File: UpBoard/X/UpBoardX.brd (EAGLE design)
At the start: 100 x 80 mm, 112 parts, among them CN1 100nF, CN2 100nF, CN3 100nF, CN4 100nF, IC1 SAM3X8E(ARDUINO), Q1 FDS5680, Q2 FDS5680, Q3 FDS5680, Q4 FDS5680

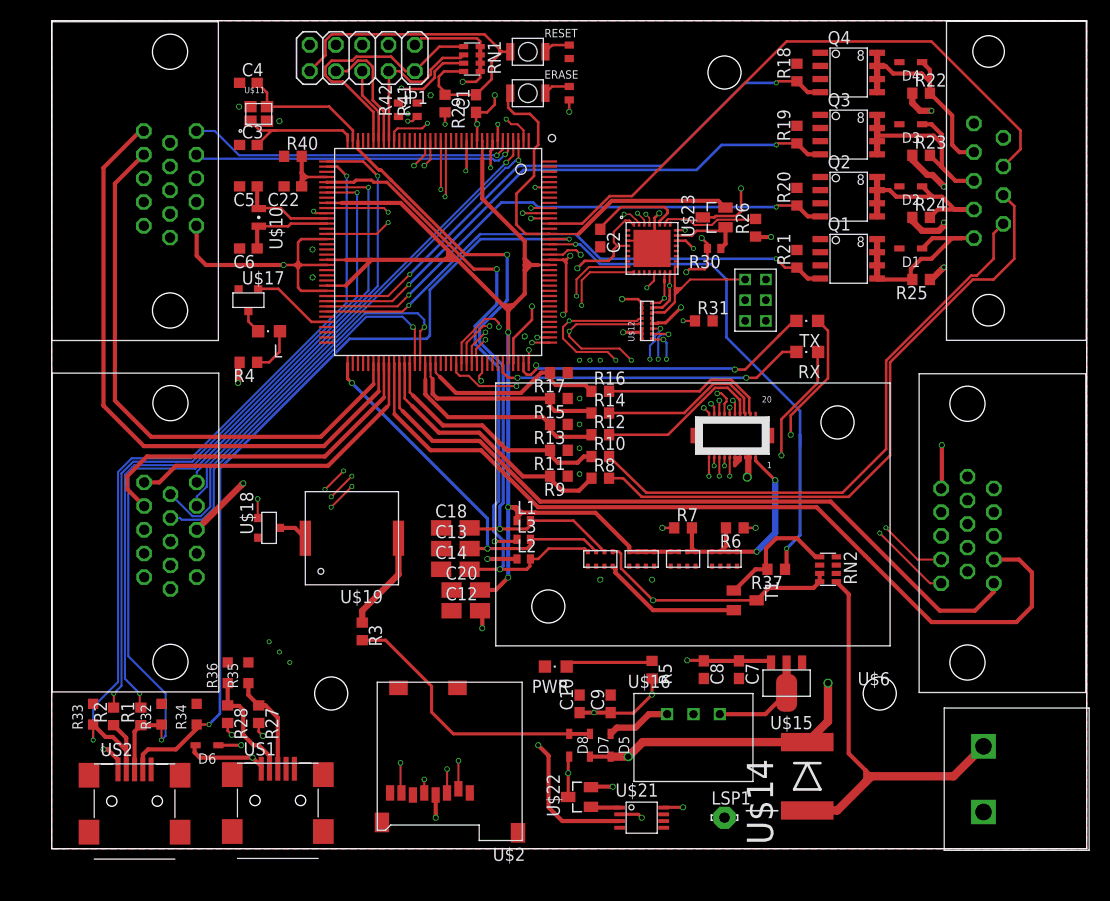
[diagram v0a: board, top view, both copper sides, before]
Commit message: Revised overly complicated power system
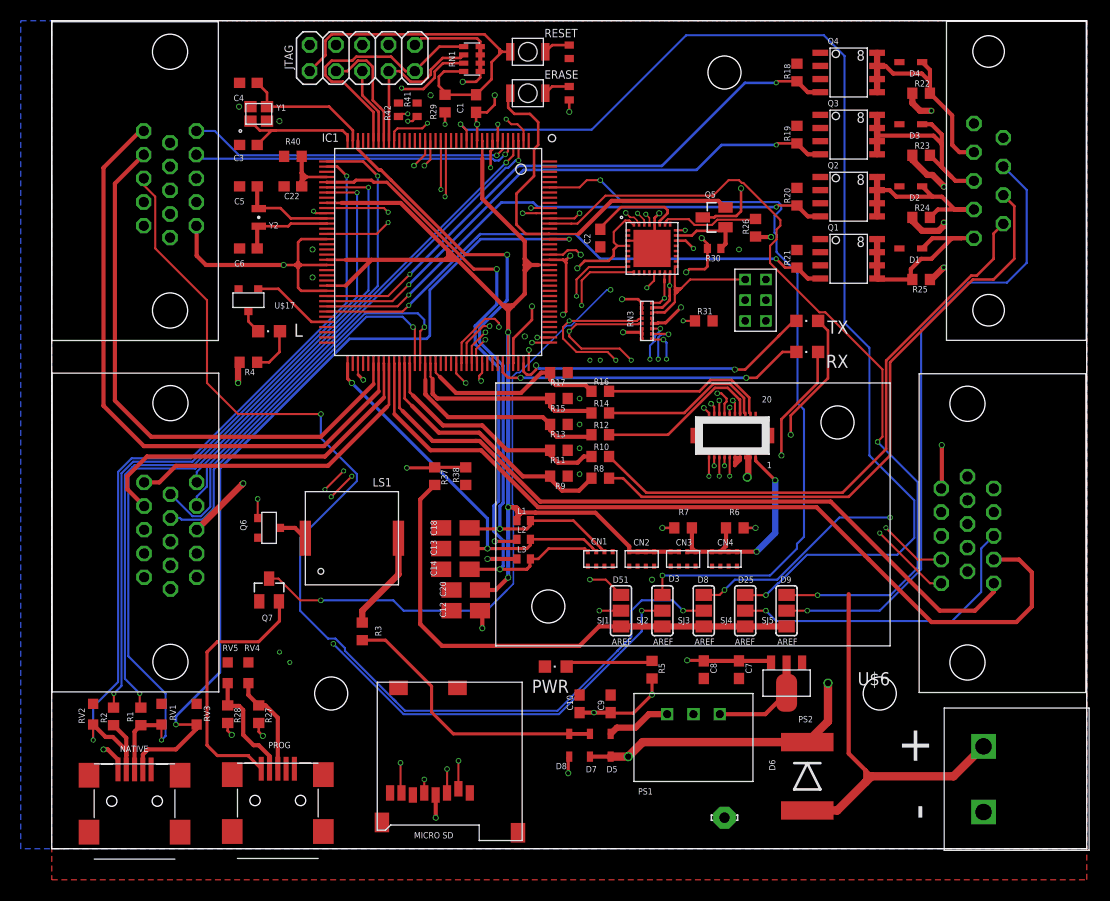
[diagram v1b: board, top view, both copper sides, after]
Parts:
- removed RN2: CTS742C083, resistor-net:CTS742C083
- removed T1: (no value), transistor:SOT23-BEC
- removed U$14: S10M-TP, UpBoard:DO-214AB
- removed U$21: OPAIC, linear:MICRO8
- removed U$22: SSMJ328R,LF, transistor-fet:SOT23
- added Q7: SSMJ328R,LF, transistor-fet:SOT23
- added R38: (no value), resistor:R0603
- added SJ1, SJ2, SJ3, SJ4, SJ5: (no value), jumper:SJ_2
- D6: value (none) -> S10M-TP; device zetex:SOD323 -> UpBoard:DO-214AB
- R37: value 1k -> (none)
- RN1: value CTS742C083 -> 10K
- RN3: value EXB-2HV102JV -> 1K
- moved D6 58.1 mm to (73.0, 7.00), turned to 90 degrees
- moved R37 34.2 mm to (37.0, 36.0), turned to 270 degrees
- moved CN4 12.0 mm to (65.0, 28.0), turned to 0 degrees
- moved CN1 4.00 mm to (53.0, 28.0), turned to 180 degrees
- moved CN2 4.00 mm to (57.0, 28.0)
- moved CN3 4.00 mm to (61.0, 28.0)
- moved L2 1.90 mm to (45.6, 29.9)
- moved L3 1.90 mm to (45.6, 28.0)
- renumbered R32 to RV1, R33 to RV2, R34 to RV3, R35 to RV4, R36 to RV5, U$10 to Y2, U$11 to Y1, U$12 to RN3, U$15 to PS2, U$16 to PS1, U$18 to Q6, U$19 to LS1, U$23 to Q5, US1 to PROG, US2 to NATIVE
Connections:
- removed net CMP: CN4.P$5, RN2.3, RN2.4, T1.C, U$21.3
- removed net CMP_GATE: R37.2, RN2.1, T1.B
- removed net N$25: U$21.1, U$22.1
- removed net N$31: CN4.P$1, T1.E
- new net AREF: R37.2, SJ1.3, SJ2.3, SJ3.3, SJ4.3, SJ5.3
- new net AREF0/D51: SJ1.2, U$6.P$16
- new net AREF1/D3: SJ2.2, U$3.13
- new net AREF2/D8: SJ3.2, U$4.13
- new net AREF3/D25: SJ4.2, U$8.13
- new net AREF4/D9: SJ5.2, U$5.7
- new net AVDREF: IC1.P$75, R37.1, R38.2
- new net N$5: Q7.3, U$1.P31
- net 1.8V: now also CN2.P$3, CN2.P$4, CN3.P$1, CN3.P$2; no longer CN1.P$1, CN1.P$2, CN1.P$3, CN1.P$4
- net 12V: now also D6.-; no longer U$14.-
- net 3.3V: now also CN4.P$1, CN4.P$2, CN4.P$3, CN4.P$4; no longer CN2.P$3, CN2.P$4, CN3.P$1, CN3.P$2, U$21.2
- net 5V: no longer D6.1, U$21.8, U$22.3
- net D25: now also SJ4.1; no longer U$8.13
- net D3: now also SJ2.1; no longer U$3.13
- net D51: now also SJ1.1; no longer U$6.P$16
- net D8: now also SJ3.1; no longer U$4.13
- net D9: now also SJ5.1; no longer U$5.7
- net GND: now also CN1.P$2, CN1.P$3, CN1.P$4, CN4.P$5, CN4.P$6, CN4.P$7, CN4.P$8, Q7.1, R38.1; no longer CN1.P$5, CN1.P$6, CN1.P$7, CN1.P$8, CN4.P$2, CN4.P$3, CN4.P$4, RN2.6, RN2.8, U$21.4
- net UOTGVBOF: no longer R37.1
- net VBUS: no longer U$22.2
- net VBUS_CFG: now also Q7.2; no longer D6.2, U$1.P31
- net VDDANA: now also CN1.P$7, L2.2; no longer CN4.P$7, L3.2
- net VDDPLL: now also CN1.P$6; no longer CN4.P$6
- net VDDUTMI: now also CN1.P$8, L3.2; no longer CN4.P$8, L2.2
- net VIN: now also D6.+; no longer RN2.5, U$14.+
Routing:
- net AREF2/D8: track 0.00 -> 107.1 mm, vias 0 -> 2
- net N$5: track 0.00 -> 68.9 mm, vias 0 -> 3
- net AREF1/D3: track 0.00 -> 63.3 mm, vias 0 -> 2
- net AREF4/D9: track 0.00 -> 60.9 mm, vias 0 -> 1
- net CMP: track 59.1 -> 0.00 mm, vias 2 -> 0
- net VBUS_CFG: track 83.6 -> 25.4 mm, vias 4 -> 0
- net UOTGVBOF: track 51.2 -> 0.00 mm, vias 2 -> 0
- net AREF: track 0.00 -> 51.1 mm
- net D25: track 71.6 -> 111.8 mm, vias 1 -> 2
- net D8: track 47.6 -> 85.3 mm, vias 1 -> 3
- net AREF0/D51: track 0.00 -> 30.8 mm, vias 0 -> 2
- net AREF3/D25: track 0.00 -> 30.3 mm, vias 0 -> 1
- net D9: track 60.5 -> 80.1 mm, vias 0 -> 2
- net AVDREF: track 0.00 -> 17.8 mm, vias 0 -> 2
- net D3: track 59.6 -> 74.6 mm, vias 3 -> 2
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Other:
- board text added: "+"
- board text added: "-"
- board text added: "AREF"
- board text added: "CN1"
- board text added: "CN2"
- board text added: "CN3"
- board text added: "CN4"
- board text added: "D25"
- board text added: "D3"
- board text added: "D51"
- board text added: "D8"
- board text added: "D9"
- board text added: "IC1"
- board text added: "JTAG"
- board text added: "LS1"
- board text added: "MICRO SD"

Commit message: Simplified power system
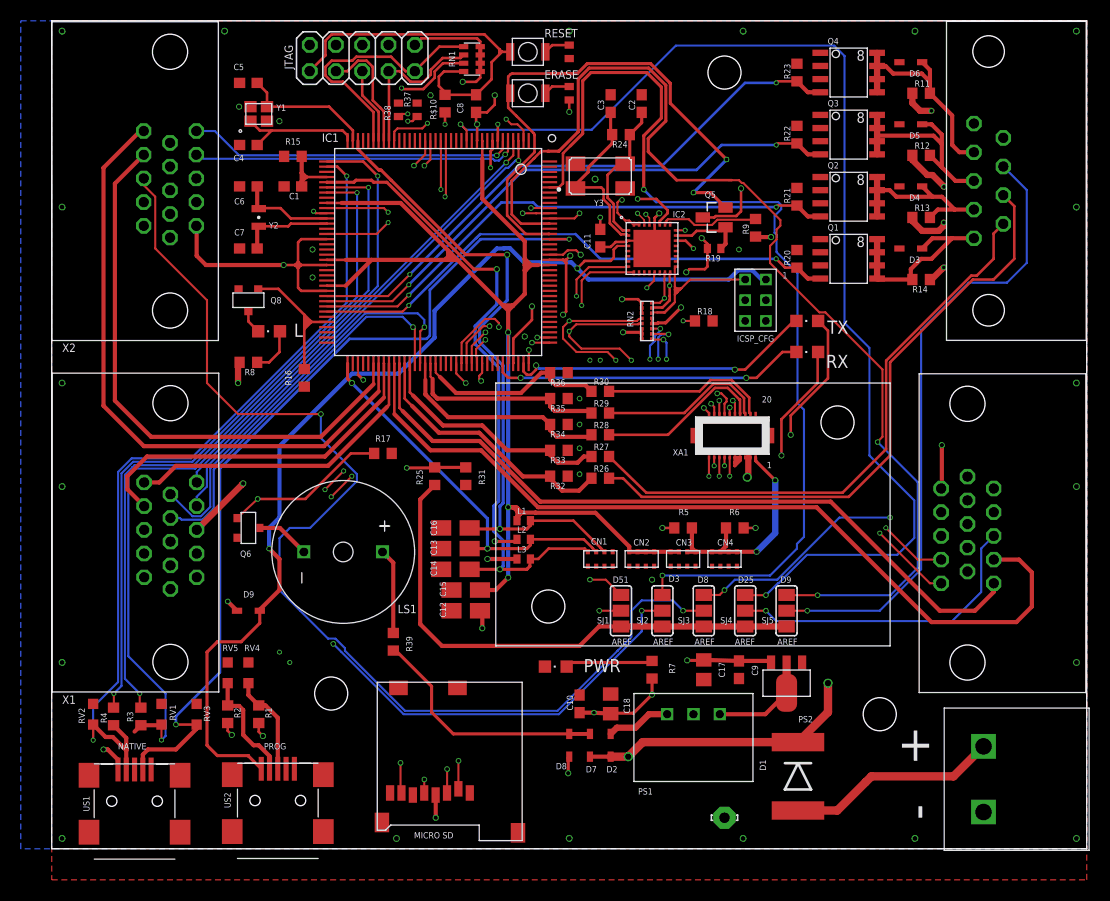
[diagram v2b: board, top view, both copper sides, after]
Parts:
- removed C20: 10uF, resistor:A/3216-18R
- removed C22: 10pF, resistor:C0603
- removed NATIVE, PROG: (no value), adafruit:USB-MINIB
- removed Q7: SSMJ328R,LF, transistor-fet:SOT23
- removed R10, R40: (no value), resistor:R0603
- removed R41, R42: 0R, resistor:R0402
- removed RN3: 1K, resistor-net:CRA-8
- removed U$1: MEGA16U2-MU, atmel:QFN32
- removed U$13: A109214, Cp2:735
- removed U$17: 2N7002E, UpBoard B:NMINI3-R1-B
- removed U$3, U$4: COMS, UpBoard B:15POSD-SUB
- removed U$5: CTRL/PYRO, UpBoard B:9POSD-SUB
- removed U$6: DF12-20PIN_CONNECTOR_HEADER, IMUPACKAGE:DF12-HEADER
- removed U$7: 2POSTERMINALBLOCK.25"PITCH, terminal_block:OSTYK22102030
- removed U$8: GP, UpBoard B:15POSD-SUB
- added C11: 1uF, resistor:C0603
- added C15, C16: 10uF, resistor:A/3216-18R
- added C17: 100uF, resistor:C0805
- added D9: (no value), zetex:SOD323
- added IC2: MEGA16U2-MU, atmel:QFN32
- added J1: 2POSTERMINALBLOCK.25"PITCH, terminal_block:OSTYK22102030
- added JP2: A109214, Cp2:735
- added Q8: 2N7002E, UpBoard B:NMINI3-R1-B
- added R$10: 1k, resistor:R0603
- added R32, R33, R34, R35, R36: (no value), resistor:R0603
- added R39: 0R, resistor:R0603
- added RN2: 1K, resistor-net:CRA-8
- added US1, US2: (no value), adafruit:USB-MINIB
- added X1, X2: COMS, UpBoard B:15POSD-SUB
- added X3: GP, UpBoard B:15POSD-SUB
- added X4: CTRL/PYRO, UpBoard B:9POSD-SUB
- added XA1: DF12-20PIN_CONNECTOR_HEADER, IMUPACKAGE:DF12-HEADER
- added Y3: 406C35D16M00000, crystal:4SMD
- C1: value (none) -> 10pF
- C10, C9: value (none) -> 100nF
- C18: value 10uF -> 100uF; device resistor:A/3216-18R -> resistor:C0805
- C2: value 1uF -> 22pF
- C3, C4, C5, C6, C7: value (none) -> 22pF
- C8: value (none) -> 10n
- D1: value (none) -> S10M-TP; device zetex:SOD323 -> UpBoard:DO-214AB
- D6: value S10M-TP -> (none); device UpBoard:DO-214AB -> zetex:SOD323
- ERASE_EN, RST_EN: value (none) -> 0R
- LS1: value PKMCS0909E4000-R1 -> AI-1440-TWT-24V-2-R; device ATFlightSecretary:PKMCS0909E400-R1 -> UpBoard:AI-1440-TWT-24-2-R
- R1, R2: value (none) -> 22
- R11, R12, R13, R14, R9: value (none) -> 1k
- R15: value (none) -> 6.8K
- R16, R17, R18, R20, R21, R22, R23: value (none) -> 10k
- R19: value (none) -> 10K; device resistor:R0603 -> resistor:R0402
- R24: value (none) -> 1M
- R26, R29: value 1k -> (none)
- R3, R4: value (none) -> 39
- R30: value 10K -> (none); device resistor:R0402 -> resistor:R0603
- R37, R38: value (none) -> 0R; device resistor:R0603 -> resistor:R0402
- R5, R6, R7, R8: value (none) -> 65
- moved D6 69.7 mm to (83.0, 76.0), turned to 180 degrees
- moved D5 66.6 mm to (83.0, 70.0), turned to 180 degrees
- moved C7 62.5 mm to (19.0, 58.0), turned to 180 degrees
- moved D2 61.3 mm to (54.0, 10.00), turned to 270 degrees
- moved C8 59.0 mm to (41.0, 72.0), turned to 90 degrees
- moved D1 52.2 mm to (72.1, 7.00), turned to 90 degrees
- moved R25 50.7 mm to (37.0, 36.0), turned to 270 degrees
- moved R11 49.1 mm to (84.0, 73.0), turned to 0 degrees
- moved R28 45.0 mm to (53.0, 40.0), turned to 0 degrees
- moved R27 41.3 mm to (53.0, 37.9), turned to 0 degrees
- moved R12 41.1 mm to (84.0, 67.0)
- moved R13 40.3 mm to (84.0, 61.0), turned to 0 degrees
- moved R4 36.6 mm to (5.97, 12.8), turned to 90 degrees
- moved R38 36.0 mm to (33.5, 71.4)
- moved R8 35.8 mm to (19.0, 47.0), turned to 180 degrees
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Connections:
- removed net N$5: Q7.3, U$1.P31
- removed net VBUS: NATIVE.VBUS, R26.1
- new net CFG_OSC2: C3.1, IC2.P2, R24.2, Y3.P1
- new net N$3: C2.1, IC2.P1, R24.1, Y3.P3
- net 1.8V: now also C15.+; no longer C20.+
- net 12V: now also D1.-, D2.2, R11.1, R12.1, R13.1, R14.1, X1.3, X2.3, X3.3, X4.1, XA1.P$2, XA1.P$3; no longer D5.2, D6.-, R22.1, R23.1, R24.1, R25.1, U$3.3, U$4.3, U$5.1, U$6.P$2, U$6.P$3, U$8.3
- net 3.3V: now also C18.1, C8.1, R19.2, R8.2, RN2.A4, RN2.A5, RN2.B1, RN2.B2, RN2.B3, X1.1, X2.1, X3.1, XA1.P$1; no longer C1.1, C9.1, R30.2, R4.2, RN3.A4, RN3.A5, RN3.B1, RN3.B2, RN3.B3, U$3.1, U$4.1, U$6.P$1, U$8.1
- net 5V: now also C17.1, C9.1, D9.1, R9.1, RN2.B6, RN2.B7, RN2.B8, US1.VBUS; no longer C7.1, C8.1, RN3.B6, RN3.B7, RN3.B8, U$1.P32, U$1.P4, U$13.P2
- net A0: now also X2.14; no longer U$4.14
- net A1: now also X2.15; no longer U$4.15
- net A10: now also R30.1, R36.2; no longer R16.1, R17.2
- net A2: now also X1.14; no longer U$3.14
- net A3: now also X1.15; no longer U$3.15
- net A4: now also X3.14; no longer U$8.14
- net A5: now also X3.15; no longer U$8.15
- net A6: now also R26.1, R32.2; no longer R8.1, R9.2
- net A7: now also R27.1, R33.2; no longer R10.1, R11.2
- net A8: now also R28.1, R34.2; no longer R12.1, R13.2
- net A9: now also R29.1, R35.2; no longer R14.1, R15.2
- net AIN10: now also R30.2, XA1.P$19; no longer R16.2, U$6.P$19
- net AIN6: now also R26.2, X4.8; no longer R8.2, U$5.8
- net AIN7: now also R27.2, X4.9; no longer R10.2, U$5.9
- net AIN8: now also R28.2, XA1.P$17; no longer R12.2, U$6.P$17
- net AIN9: now also R29.2, XA1.P$18; no longer R14.2, U$6.P$18
- net AREF: now also R25.2; no longer R37.2
- net AREF0/D51: now also XA1.P$16; no longer U$6.P$16
- net AREF1/D3: now also X1.13; no longer U$3.13
- net AREF2/D8: now also X2.13; no longer U$4.13
- net AREF3/D25: now also X3.13; no longer U$8.13
- net AREF4/D9: now also X4.7; no longer U$5.7
- net AVDREF: now also R25.1, R31.2; no longer R37.1, R38.2
- net BD+: now also R1.1, US2.D+; no longer PROG.D+, R27.1
- net BD-: now also R2.1, US2.D-; no longer PROG.D-, R28.1
- net CFG_D+: now also IC2.P29, R1.2; no longer R27.2, U$1.P29
- net CFG_D-: now also IC2.P30, R2.2; no longer R28.2, U$1.P30
- net CFG_MISO: now also IC2.P17, JP2.P1, RN2.A6; no longer RN3.A6, U$1.P17, U$13.P1
- net CFG_MOSI: now also IC2.P16, JP2.P4, RN2.A7; no longer RN3.A7, U$1.P16, U$13.P4
- net CFG_RESET: now also IC2.P24, JP2.P5; no longer U$1.P24, U$13.P5
- net CFG_SCK: now also IC2.P15, JP2.P3, RN2.A8; no longer RN3.A8, U$1.P15, U$13.P3
- net D+: now also R3.1; no longer NATIVE.D+, R1.1
- net D-: now also R4.1, US1.D-; no longer NATIVE.D-, R2.1
- net D12: now also R17.1
- net D13: now also Q8.1, R16.2; no longer U$17.1
- net D23: now also X3.11; no longer U$8.11
- net D24: now also X3.12; no longer U$8.12
- net D37: now also R23.1; no longer R18.1
- net D38: now also R22.1; no longer R19.1
- net D39: now also R21.1; no longer R20.1
- net D40: now also R20.1; no longer R21.1
- net D46: now also XA1.P$11; no longer U$6.P$11
- net D47: now also XA1.P$12; no longer U$6.P$12
- net D48: now also XA1.P$13; no longer U$6.P$13
- net D49: now also XA1.P$14; no longer U$6.P$14
- net D50: now also XA1.P$15; no longer U$6.P$15
- net D6: now also X2.11; no longer U$4.11
- net D7: now also X2.12; no longer U$4.12
- net ERASE_CMD: now also IC2.P23, R19.1; no longer R30.1, U$1.P23
- net F0/X+: now also D6.1, R11.2, X4.2; no longer D4.1, R22.2, U$5.2
- net F1/X-: now also D5.1, R12.2, X4.3; no longer D3.1, R23.2, U$5.3
- net F2/Y+: now also D4.1, R13.2, X4.4; no longer D2.1, R24.2, U$5.4
- net F3/Y-: now also D3.1, R14.2, X4.5; no longer D1.1, R25.2, U$5.5
- net GND: now also C1.2, C11.2, C15.-, C16.-, C17.2, C18.2, C3.2, C5.1, D5.2, D6.2, IC2.P28, IC2.P3, IC2.TH, J1.P$2, JP2.P6, Q8.2, R16.1, R17.2, R22.2, R23.2, R31.1, R32.1, R33.1, R34.1, R35.1, R36.1, R37.2, R38.2, US1.GND, US2.GND, X1.2, X2.2, X3.2, X4.6, XA1.P$20, XA1.P$4, XA1.P$5, Y3.P2, Y3.P4; no longer C18.-, C20.-, C22.2, C3.1, C5.2, C8.2, D1.2, D2.2, NATIVE.GND, PROG.GND, Q7.1, R11.1, R13.1, R17.1, R19.2, R31.2, R38.1, R40.1, R41.2, R42.2, R9.1, U$1.P28, U$1.P3, U$1.TH, U$13.P6, U$17.2, U$3.2, U$4.2, U$5.6, U$6.P$20, U$6.P$4, U$6.P$5, U$7.P$2, U$8.2
- net HV: now also R39.2; no longer R3.2
- net JTAG_SEL: now also R38.1; no longer R42.1
- net MISO: now also RN2.A1, X1.6, X2.6, X3.6, XA1.P$6; no longer RN3.A1, U$3.6, U$4.6, U$6.P$6, U$8.6
- net MOSI: now also RN2.A2, X1.7, X2.7, X3.7, XA1.P$7; no longer RN3.A2, U$3.7, U$4.7, U$6.P$7, U$8.7
- net M_RESET: now also C8.2, R$10.1; no longer C1.2, R29.1
- net N$1: now also C11.1, IC2.P27; no longer C2.1, U$1.P27
- net N$11: now also IC2.P26, R9.2; no longer R26.2, U$1.P26
- net N$2: now also R3.2; no longer R1.2
- net N$20: now also IC2.P22, R$10.2; no longer R29.2, U$1.P22
- net N$23: now also IC2.P13, R18.1; no longer R31.1, U$1.P13
- net N$32: now also C5.2; no longer C4.2
- net N$33: now also LS1.-; no longer LS1.P2
- net N$34: now also C4.2; no longer C3.2
- net N$35: now also C7.1; no longer C6.1
- net N$36: now also C6.1; no longer C5.1
- net N$38: now also Q8.3; no longer U$17.3
- net N$39: now also LS1.+, R39.1; no longer LS1.P1, R3.1
- net N$40: now also R8.1; no longer R4.1
- net N$41: now also C1.1, R15.2; no longer C22.1, R40.2
- net N$42: now also R7.1; no longer R5.1
- net N$44: now also R5.1; no longer R7.1
- net N$7: now also D2.1; no longer D5.1
- net N$9: now also R4.2; no longer R2.2
- net RX/D0: now also IC2.P9, X3.4; no longer U$1.P9, U$8.4
- net RX1: now also X1.4; no longer U$3.4
- net RX2: now also X2.4; no longer U$4.4
- net RX3/D15: now also X1.11; no longer U$3.11
- net SCK: now also RN2.A3, X1.8, X2.8, X3.8, XA1.P$8; no longer RN3.A3, U$3.8, U$4.8, U$6.P$8, U$8.8
- net SCL: now also RN2.B5, X1.10, X2.10, X3.10, XA1.P$10; no longer RN3.B5, U$3.10, U$4.10, U$6.P$10, U$8.10
- net SDA: now also RN2.B4, X1.9, X2.9, X3.9, XA1.P$9; no longer RN3.B4, U$3.9, U$4.9, U$6.P$9, U$8.9
- net TST: now also R37.1; no longer R41.1
- net TX/D1: now also IC2.P8, X3.5; no longer U$1.P8, U$8.5
- net TX1: now also X1.5; no longer U$3.5
- net TX2: now also X2.5; no longer U$4.5
- net TX3/D14: now also X1.12; no longer U$3.12
- net UOTGID: now also US1.ID; no longer NATIVE.ID
- net VBUS_CFG: now also D9.2, IC2.P31, IC2.P32, IC2.P4, JP2.P2, US2.VBUS; no longer PROG.VBUS, Q7.2
- net VDDPLL: now also C16.+; no longer C18.+
- net VIN: now also D1.+, J1.P$1; no longer D6.+, U$7.P$1
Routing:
- net VBUS: track 158.6 -> 0.00 mm, vias 2 -> 0
- net 5V: track 23.2 -> 172.9 mm, vias 4 -> 6
- net VBUS_CFG: track 25.4 -> 118.3 mm, vias 0 -> 3
- net D23: track 179.7 -> 105.3 mm
- net N$5: track 68.9 -> 0.00 mm, vias 3 -> 0
- net D9: track 80.1 -> 107.8 mm
- net D3: track 74.6 -> 99.7 mm
- net VIN: track 39.3 -> 20.6 mm
- net CFG_OSC2: track 0.00 -> 17.5 mm
- net N$21: track 38.0 -> 55.4 mm, vias 0 -> 2
- net N$3: track 0.00 -> 14.2 mm
- net D12: track 47.3 -> 61.2 mm
- net D13: track 7.96 -> 16.5 mm
- net D+: track 83.0 -> 79.4 mm
- net HV: track 29.2 -> 25.8 mm
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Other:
- board text added: "1"
- board text added: "10/2017"
- board text added: "Cal Poly Space Systems"
- board text added: "Designed by: Patrick Chizek Harrison King Brett Glidden"
- board text added: "IC2"
- board text added: "ICSP_CFG"
- board text added: "NATIVE"
- board text added: "PROG"
- board text added: "X1"
- board text added: "X2"
- board text added: "XA1"
- board text added: "Y3"
- board text removed: "C:/Users/Patrick Chizek/Pictures/UBXlogo.bmp"
- board text removed: "LS1"

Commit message: Re-centered Dimensions
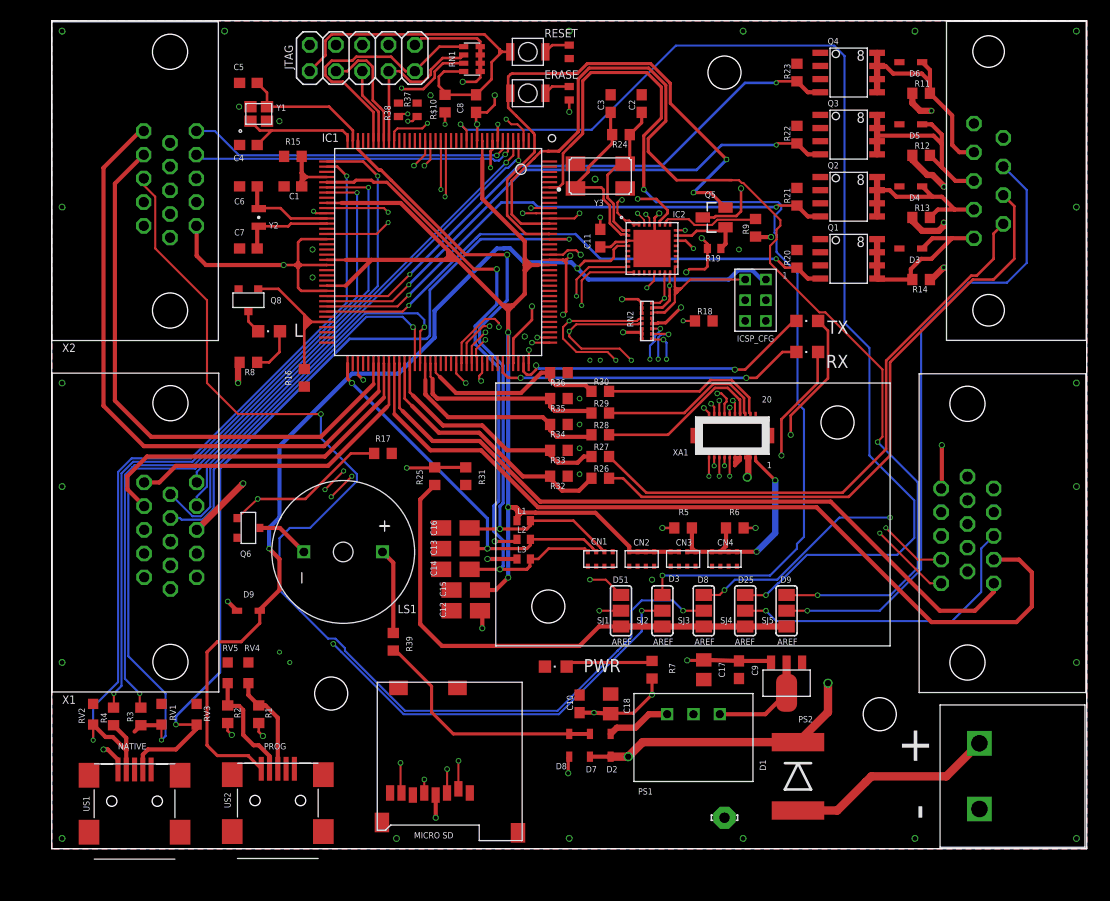
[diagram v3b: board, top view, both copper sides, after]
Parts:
- moved J1 0.50 mm to (89.6, 7.02)
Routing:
- net D23: track 105.3 -> 90.2 mm

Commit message: Finished labeling, removed SPI pull ups
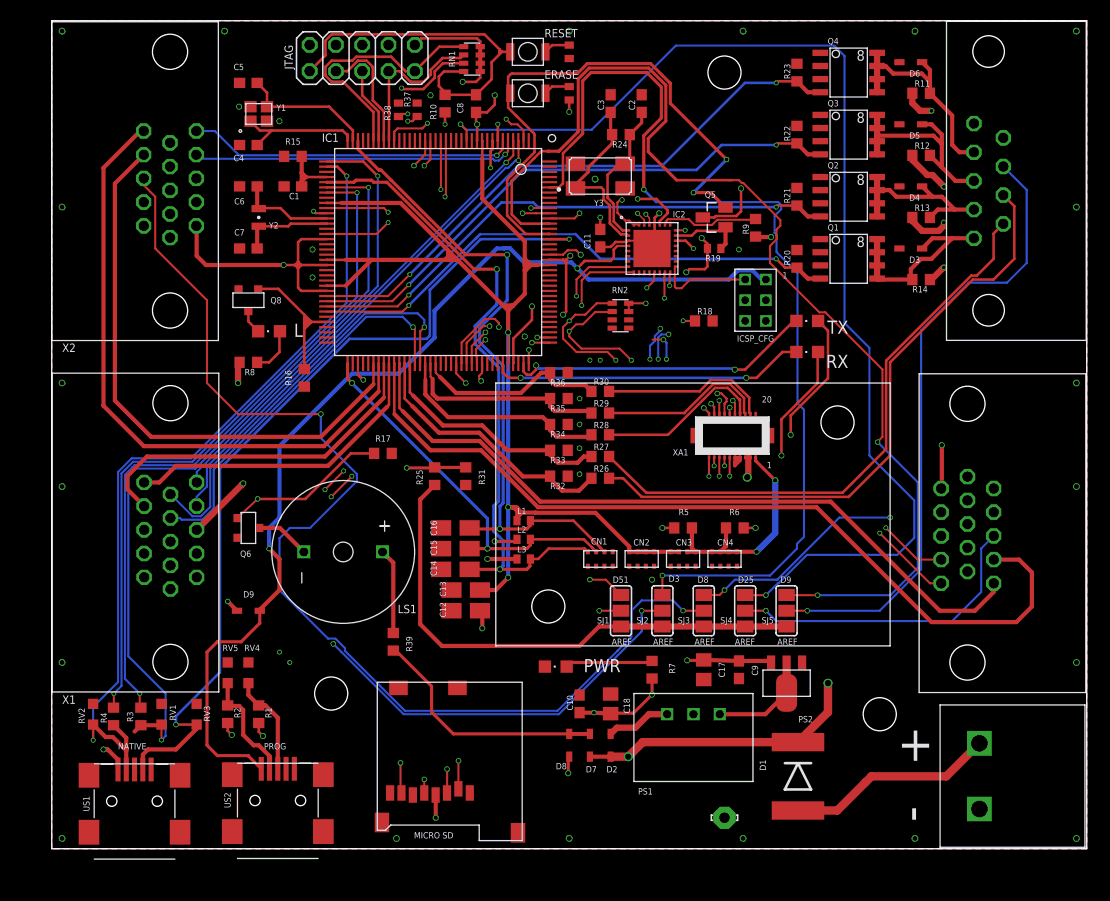
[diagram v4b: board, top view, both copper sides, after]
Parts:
- RN2: value 1K -> 1k; device resistor-net:CRA-8 -> resistor-net:CTS742C083
- moved C13 4.12 mm to (40.0, 25.0)
- moved C15 4.12 mm to (39.0, 29.0)
- moved RN2 2.60 mm to (55.0, 51.5), turned to 270 degrees
- renumbered R$10 to R10
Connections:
- net 1.8V: now also C13.+; no longer C15.+
- net 3.3V: now also RN2.7, RN2.8; no longer RN2.A4, RN2.A5, RN2.B1, RN2.B2, RN2.B3
- net 5V: no longer RN2.B6, RN2.B7, RN2.B8
- net CFG_MISO: no longer RN2.A6
- net CFG_MOSI: no longer RN2.A7
- net CFG_SCK: no longer RN2.A8
- net MISO: no longer RN2.A1
- net MOSI: no longer RN2.A2
- net SCK: no longer RN2.A3
- net SCL: now also RN2.1; no longer RN2.B5
- net SDA: now also RN2.2; no longer RN2.B4
- net VDDANA: now also C15.+; no longer C13.+
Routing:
- net CFG_MISO: track 15.1 -> 9.22 mm
- net 3.3V: track 136.7 -> 132.3 mm, vias 23 -> 22
- net CFG_MOSI: track 15.2 -> 11.8 mm
- net 5V: track 172.9 -> 169.8 mm, vias 6 -> 5
- net SDA: track 148.3 -> 145.9 mm
- net SCL: track 156.4 -> 154.1 mm
- net MOSI: track 184.9 -> 183.4 mm
- net CFG_SCK: track 11.8 -> 10.4 mm
- net SCK: track 183.4 -> 182.6 mm
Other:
- board text added: "15"
- board text added: "15-DSUB PINOUT"
- board text added: "3.3V"
- board text added: "9"
- board text added: "9-DSUB PINOUT"
- board text added: "AIN6"
- board text added: "AIN7"
- board text added: "AIN_A"
- board text added: "AIN_B"
- board text added: "AREF/D9"
- board text added: "AREF/D_C"
- board text added: "D_A"
- board text added: "D_B"
- board text added: "GND"
- board text added: "HV"
- board text added: "HVOUT_0"
- board text added: "HVOUT_1"
- board text added: "HVOUT_2"
- board text added: "HVOUT_3"
- board text added: "MISO"
- board text added: "MOSI"
- board text added: "RX"
- board text added: "SCK"
- board text added: "SCL"
- board text added: "SDA"
- board text added: "TX"
